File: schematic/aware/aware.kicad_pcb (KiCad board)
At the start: 2 copper layers, 66 x 76.2 mm, 32 parts, among them J1 Servo_Conn, J2 Nowcast_LEDS_Conn, J3 Forcast_LEDS_Conn, J4 Battery_Conn, Q1 BC548, U1 Solar_Charger, U2 LM393

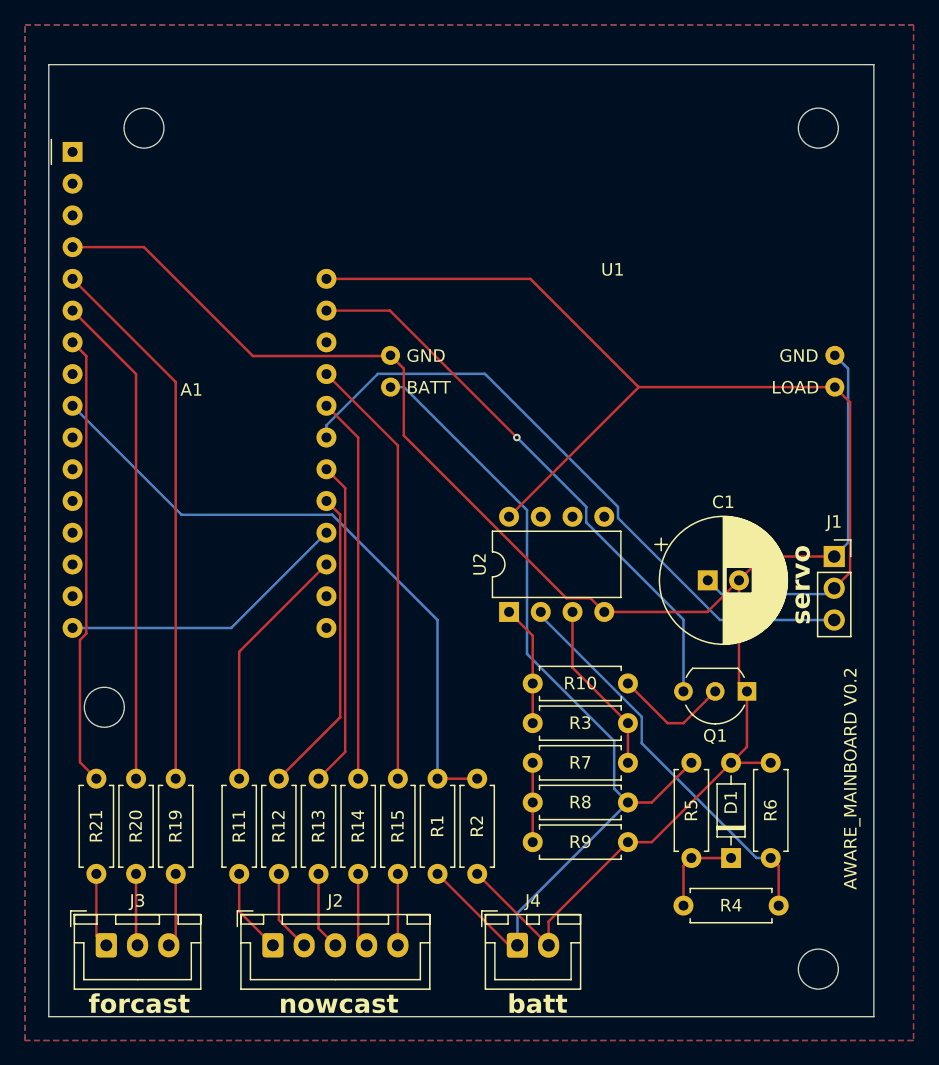
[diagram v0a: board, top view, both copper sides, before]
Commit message: adjusted pinout of forcast connector on mainboard
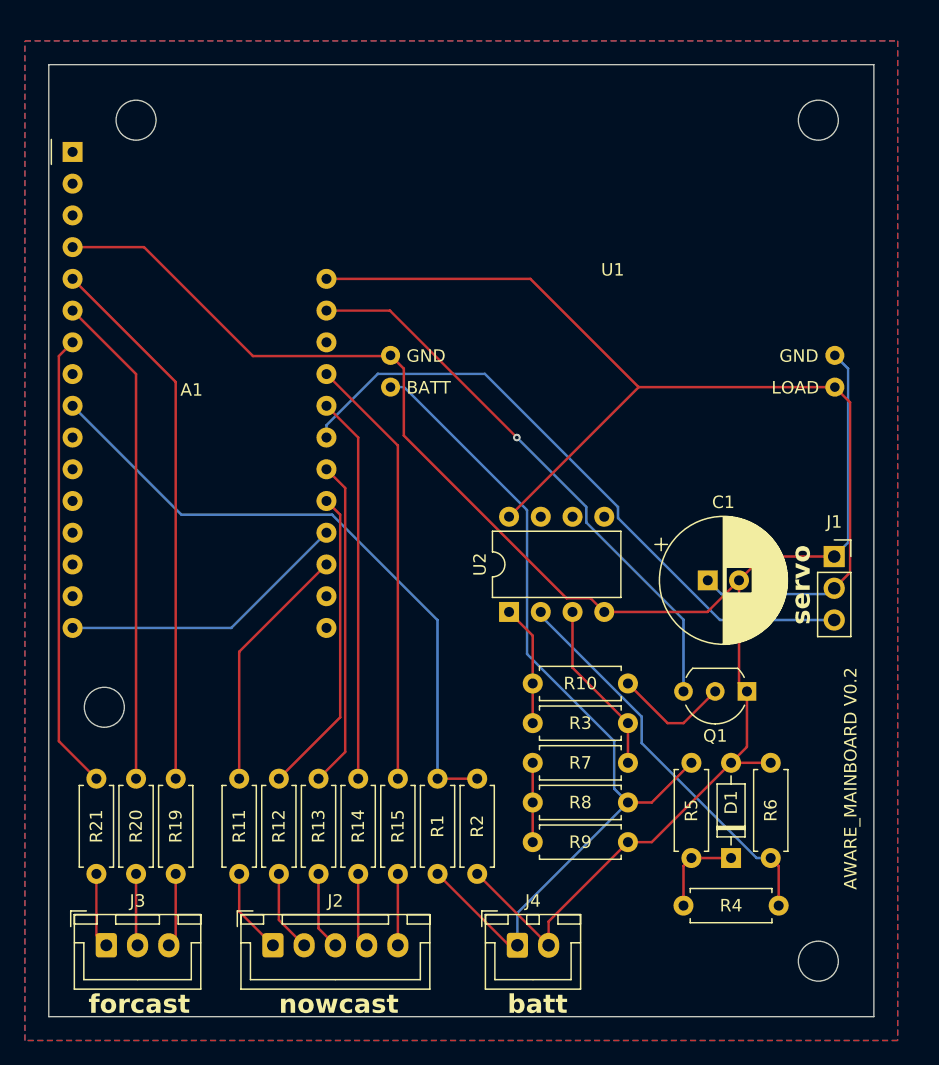
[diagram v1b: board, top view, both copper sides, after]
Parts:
- removed the REF** at (104.8, 36.2)
- removed the REF** at (101.6, 82.5)
- removed the REF** at (158.8, 103.5)
- removed the REF** at (158.8, 36.2)
- added REF**: MountingHole_3.2mm_M3, MountingHole:MountingHole_3.2mm_M3, F.Cu at (158.8, 35.6)
- added REF**: MountingHole_3.2mm_M3, MountingHole:MountingHole_3.2mm_M3, F.Cu at (101.6, 82.5)
- added REF**: MountingHole_3.2mm_M3, MountingHole:MountingHole_3.2mm_M3, F.Cu at (158.8, 102.9)
- added REF**: MountingHole_3.2mm_M3, MountingHole:MountingHole_3.2mm_M3, F.Cu at (104.1, 35.6)
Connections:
- A1 pad 5: FUTURE_LED_A -> FUTURE_LED_C
- A1 pad 7: FUTURE_LED_C -> FUTURE_LED_A
- R19 pad 2: FUTURE_LED_A -> FUTURE_LED_C
- R21 pad 2: FUTURE_LED_C -> FUTURE_LED_A
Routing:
- net FUTURE_LED_C: track 36.1 -> 43.4 mm
- net FUTURE_LED_A: track 43.4 -> 36.6 mm

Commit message: added minor fixes and updated gerbers
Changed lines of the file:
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@@
       (plot_on_all_layers_selection 0x0000000_00000000)
       (disableapertmacros false)
-      (usegerberextensions false)
-      (usegerberattributes true)
-      (usegerberadvancedattributes true)
-      (creategerberjobfile true)
+      (usegerberextensions true)
+      (usegerberattributes false)
+      (usegerberadvancedattributes false)
+      (creategerberjobfile false)
       (dashed_line_dash_ratio 12.000000)
       (dashed_line_gap_ratio 3.000000)
@@
       (plotinvisibletext false)
       (sketchpadsonfab false)
-      (subtractmaskfromsilk false)
+      (subtractmaskfromsilk true)
       (outputformat 1)
       (mirror false)
-      (drillshape 1)
+      (drillshape 0)
       (scaleselection 1)
-      (outputdirectory "")
+      (outputdirectory "gerbers/")
     )
   )
@@
     (fp_line (start 4.95 3.4) (end 4.95 -2.35)
       (stroke (width 0.1) (type solid)) (layer "F.Fab"))
-    (pad "1" thru_hole roundrect (at 0 0) (size 1.7 2) (drill 1) (layers "*.Cu" "*.Mask") (roundrect_rratio 0.147059)
+    (pad "1" thru_hole roundrect (at 0 0) (size 1.7 2) (drill 1) (layers "*.Cu" "*.Mask") (roundrect_rratio 0.1470588235)
       (net 29 "Vbat") (pinfunction "Pin_1") (pintype "passive"))
     (pad "2" thru_hole oval (at 2.5 0) (size 1.7 2) (drill 1) (layers "*.Cu" "*.Mask")
@@
     (fp_line (start 7.45 3.4) (end 7.45 -2.35)
       (stroke (width 0.1) (type solid)) (layer "F.Fab"))
-    (pad "1" thru_hole roundrect (at 0 0) (size 1.7 1.95) (drill 0.95) (layers "*.Cu" "*.Mask") (roundrect_rratio 0.147059)
+    (pad "1" thru_hole roundrect (at 0 0) (size 1.7 1.95) (drill 0.95) (layers "*.Cu" "*.Mask") (roundrect_rratio 0.1470588235)
       (net 42 "Net-(J3-Pin_1)") (pinfunction "Pin_1") (pintype "passive"))
     (pad "2" thru_hole oval (at 2.5 0) (size 1.7 1.95) (drill 0.95) (layers "*.Cu" "*.Mask")
@@
     (fp_line (start 12.45 3.4) (end 12.45 -2.35)
       (stroke (width 0.1) (type solid)) (layer "F.Fab"))
-    (pad "1" thru_hole roundrect (at 0 0) (size 1.7 1.95) (drill 0.95) (layers "*.Cu" "*.Mask") (roundrect_rratio 0.147059)
+    (pad "1" thru_hole roundrect (at 0 0) (size 1.7 1.95) (drill 0.95) (layers "*.Cu" "*.Mask") (roundrect_rratio 0.1470588235)
       (net 41 "Net-(J2-Pin_1)") (pinfunction "Pin_1") (pintype "passive"))
     (pad "2" thru_hole oval (at 2.5 0) (size 1.7 1.95) (drill 0.95) (layers "*.Cu" "*.Mask")
